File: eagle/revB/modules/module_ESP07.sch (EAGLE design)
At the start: 23 parts

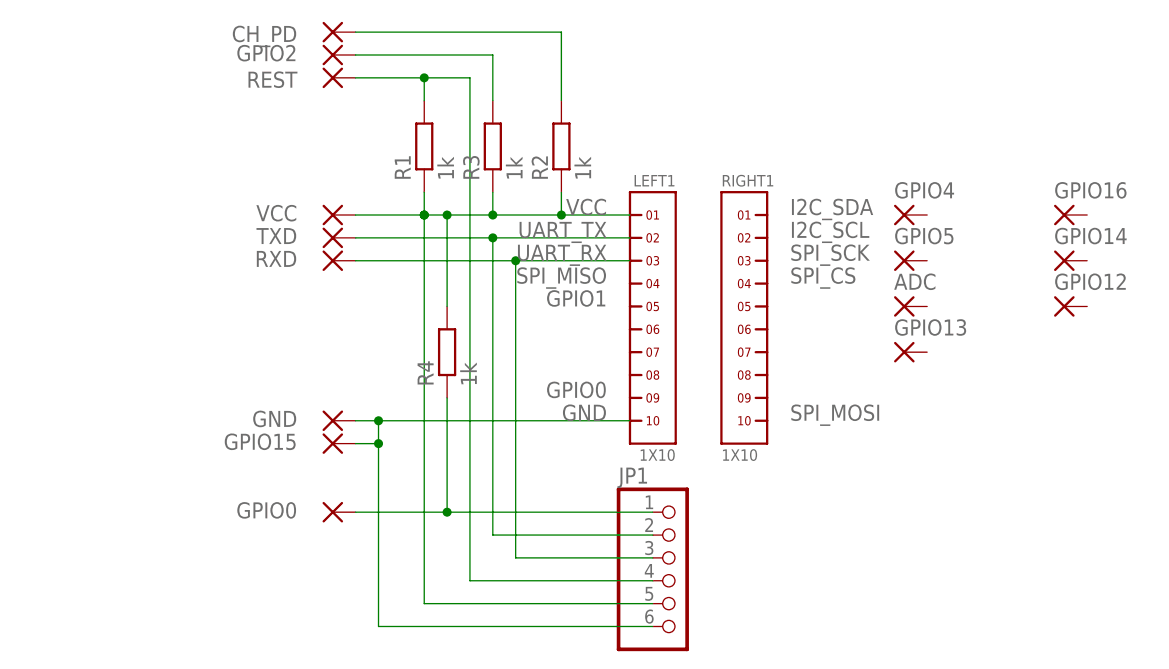
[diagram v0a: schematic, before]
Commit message: ESP8266 - Added indication LEDs
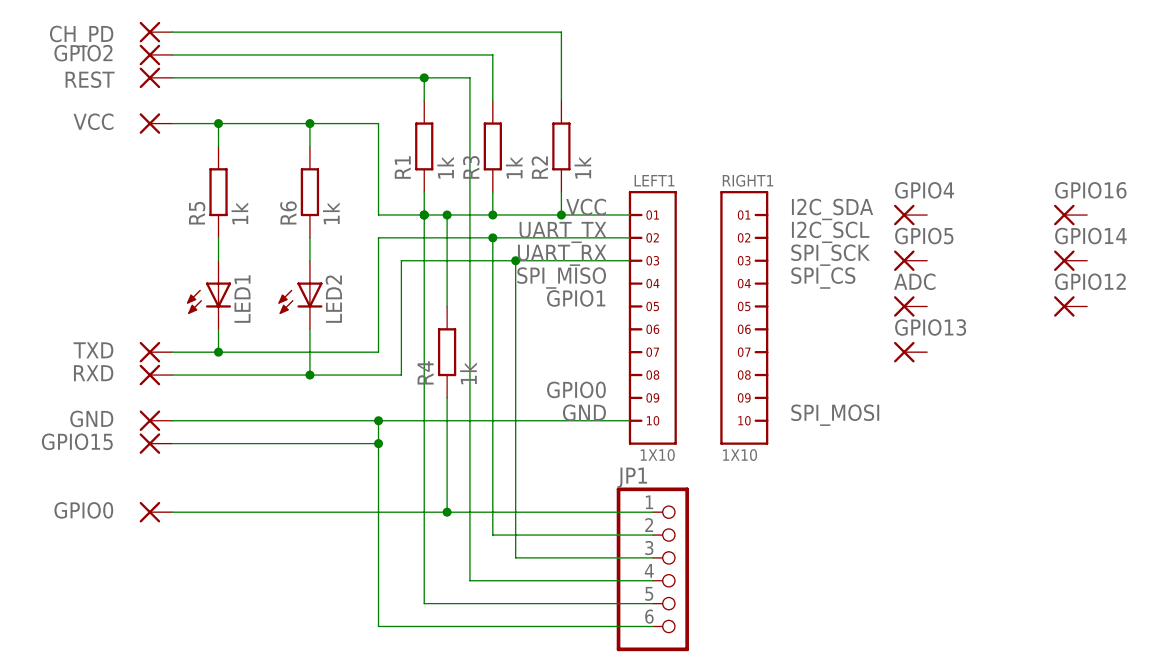
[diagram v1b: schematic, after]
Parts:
- added LED1, LED2: (no value), led:LEDCHIPLED_0603
- added R5, R6: 1k, rcl:R-EU_R0603
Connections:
- new net N$3: LED2.A, R6.1
- new net N$4: LED1.A, R5.1
- net UART_RX: now also LED2.C
- net UART_TX: now also LED1.C
- net VCC: now also R5.2, R6.2
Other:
- moved on the sheet: CH_PD, GND, GPIO0, GPIO15, GPIO2, REST, RXD, TXD, VCC
